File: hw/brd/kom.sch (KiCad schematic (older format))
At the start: 102 parts, among them IC1 ATMEGA328-P, IC2 4067D, IC3 L293D, J1 EXT, K1 CONN_3, M1 XBEE, P1 Serial, P10 GPIO_4PIN, P11 GPIO_4PIN, P12 GPIO_4PIN, P13 GPIO_4PIN, P14 GPIO_4PIN, P15 GPIO_4PIN, P16 GPIO_4PIN, P2 GPIO_4PIN, P3 GPIO_4PIN, P4 GPIO_4PIN, P5 GPIO_4PIN, P6 GPIO_4PIN, P7 GPIO_4PIN, P8 IR_Scanner, P9 GPIO_4PIN, Q1 PT480F, Q2 PT480F, Q3 PT480F, Q4 PT480F, SW1 SW_RESET, SW2 PwrOn, SW3 PWR_Control, SW4 TEST, U1 INDUCTOR, U2 LM7833, U3 74LS125, U4 TC54, U5 PTH08000WAZT, U6 ULN2003A, X1 16MHz

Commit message: - Changed schematic notation - Standard footprints linked
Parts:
- removed BypCCap2: MotorR, symbol C
- removed SW1: SW_RESET, symbol SW_PUSH
- removed SW4: TEST, symbol SW_PUSH
- added C?: 100nF MotorR, symbol C
- added SW1: SW_RESET, symbol PULSADOR
- added SW4: TEST, symbol PULSADOR
- C?: renamed from BypCCap1; value MotorL -> 100nF MotorL
- CAP?: renamed from H_Cap1; value 100uF -> 100uF HBridge
- CAP?: renamed from IR_Cap1; value 10uF -> 10uF IR
- CAP?: renamed from US_Cap1; value 10uF -> 10uF US
- CAP?: renamed from Mux_Cap1; value 100nF -> 100nF Mux
- CAP?: renamed from InCap1; value 100uF -> 100uF InCap
- CAP?: renamed from RadioCCap1; value 8.2pF -> 8.2pF Radio
- CAP?: renamed from RadioECap1; value 1uF -> 1uF Radio
- CAP?: renamed from AVCC_Cap1; value 100n -> 100n AVCC
- CAP?: renamed from AVR_Cap1; value 100n -> 100n AVR
- InvPolDiode1: value 200mA min -> 200mA IPP
- J?: renamed from K1; value CONN_3 -> LiPo
- P?: renamed from AREF1; value CONN_1 -> ARef
- renumbered I2 to I2C?, I1 to I2C?
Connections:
- wire segments 350 -> 267

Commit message: - Created new modules: 	Bluetooth 	LED_IR_Side 	JST_XH 	IR_PHT_Side 	PTH08000 	Ultrasonic sensor - Associated components
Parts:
- gave numbers to parts that had none: 15
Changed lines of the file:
@@
-EESchema Schematic File Version 2  date Mon 25 Jun 2012 08:07:17 PM CEST
+EESchema Schematic File Version 2  date Mon 25 Jun 2012 08:58:39 PM CEST
 LIBS:power
 LIBS:device
@@
 $EndComp
 $Comp
-L CONN_1 P?
+L CONN_1 P17
 U 1 1 4FD082B3
 P 3000 5000
-F 0 "P?" H 3080 5000 40  0000 L CNN
+F 0 "P17" H 3080 5000 40  0000 L CNN
 F 1 "ARef" H 3000 5055 29  0000 C CNN
 	1    3000 5000
@@
 $EndComp
 $Comp
-L JP_4 I2C?
+L JP_4 I2C2
 U 1 1 4FE2F5BD
 P 2750 9800
-F 0 "I2C?" H 2910 10020 58  0000 C CNN
+F 0 "I2C2" H 2910 10020 58  0000 C CNN
 F 1 "JP_4" H 2900 9740 60  0001 C CNN
 	1    2750 9800
@@
 $EndComp
 $Comp
-L JP_4 I2C?
+L JP_4 I2C1
 U 1 1 4FE2F5D4
 P 2250 9800
-F 0 "I2C?" H 2410 10020 58  0000 C CNN
+F 0 "I2C1" H 2410 10020 58  0000 C CNN
 F 1 "JP_4" H 2400 9740 60  0001 C CNN
 	1    2250 9800
@@
 $EndComp
 $Comp
-L CPOL CAP?
+L CPOL CAP3
 U 1 1 4FE2FF90
 P 8850 6750
-F 0 "CAP?" H 8950 6900 50  0000 L CNN
+F 0 "CAP3" H 8950 6900 50  0000 L CNN
 F 1 "100uF HBridge" H 8750 6600 50  0000 L CNN
 	1    8850 6750
@@
 $EndComp
 $Comp
-L CPOL CAP?
+L CPOL CAP2
 U 1 1 4FE2FF96
 P 8450 6750
-F 0 "CAP?" H 8550 6900 50  0000 L CNN
+F 0 "CAP2" H 8550 6900 50  0000 L CNN
 F 1 "10uF IR" H 8500 6600 50  0000 L CNN
 	1    8450 6750
@@
 $EndComp
 $Comp
-L CPOL CAP?
+L CPOL CAP4
 U 1 1 4FE2FFB0
 P 9250 6750
-F 0 "CAP?" H 9350 6900 50  0000 L CNN
+F 0 "CAP4" H 9350 6900 50  0000 L CNN
 F 1 "10uF US" H 9300 6600 50  0000 L CNN
 	1    9250 6750
@@
 $EndComp
 $Comp
-L CPOL CAP?
+L CPOL CAP5
 U 1 1 4FE2FFB6
 P 9650 6750
-F 0 "CAP?" H 9750 6900 50  0000 L CNN
+F 0 "CAP5" H 9750 6900 50  0000 L CNN
 F 1 "100nF Mux" H 9650 6600 50  0000 L CNN
 	1    9650 6750
@@
 	8450 6300 8450 6400
 $Comp
-L C C?
+L C C5
 U 1 1 4FE84566
 P 13250 9400
-F 0 "C?" V 13100 9350 50  0000 L CNN
+F 0 "C5" V 13100 9350 50  0000 L CNN
 F 1 "100nF MotorL" V 13400 9150 50  0000 L CNN
 	1    13250 9400
@@
 Connection ~ 15250 9700
 $Comp
-L CONN_3 J?
+L CONN_3 J2
 U 1 1 4FE85361
 P 1200 2200
-F 0 "J?" V 1150 2200 50  0000 C CNN
+F 0 "J2" V 1150 2200 50  0000 C CNN
 F 1 "LiPo" V 1250 2200 40  0000 C CNN
 	1    1200 2200
@@
 $EndComp
 $Comp
-L CPOL CAP?
+L CPOL CAP1
 U 1 1 4FE85957
 P 4650 2050
-F 0 "CAP?" H 4700 2200 50  0000 L CNN
+F 0 "CAP1" H 4700 2200 50  0000 L CNN
 F 1 "100uF InCap" H 4650 1900 50  0000 L CNN
 	1    4650 2050
@@
 	9650 6300 9650 6400
 $Comp
-L C CAP?
+L C CAP9
 U 1 1 4FE85D74
 P 11300 6550
-F 0 "CAP?" V 11150 6400 50  0000 L CNN
+F 0 "CAP9" V 11150 6400 50  0000 L CNN
 F 1 "8.2pF Radio" V 11450 6300 50  0000 L CNN
 	1    11300 6550
@@
 $EndComp
 $Comp
-L CPOL CAP?
+L CPOL CAP8
 U 1 1 4FE85D81
 P 10900 6750
-F 0 "CAP?" H 11000 6900 50  0000 L CNN
+F 0 "CAP8" H 11000 6900 50  0000 L CNN
 F 1 "1uF Radio" H 10900 6600 50  0000 L CNN
 	1    10900 6750
@@
 $EndComp
 $Comp
-L C CAP?
+L C CAP7
 U 1 1 4FE85DC0
 P 10500 6550
-F 0 "CAP?" V 10350 6450 50  0000 L CNN
+F 0 "CAP7" V 10350 6450 50  0000 L CNN
 F 1 "100n AVCC" V 10650 6350 50  0000 L CNN
 	1    10500 6550
@@
 Connection ~ 10900 6850
 $Comp
-L C CAP?
+L C CAP6
 U 1 1 4FE874B6
 P 10100 6550
-F 0 "CAP?" V 9950 6450 50  0000 L CNN
+F 0 "CAP6" V 9950 6450 50  0000 L CNN
 F 1 "100n AVR" V 10250 6350 50  0000 L CNN
 	1    10100 6550
@@
 $EndComp
 $Comp
-L C C?
+L C C6
 U 1 1 4FE8BAFD
 P 15250 9400
-F 0 "C?" V 15100 9350 50  0000 L CNN
+F 0 "C6" V 15100 9350 50  0000 L CNN
 F 1 "100nF MotorR" V 15400 9150 50  0000 L CNN
 	1    15250 9400

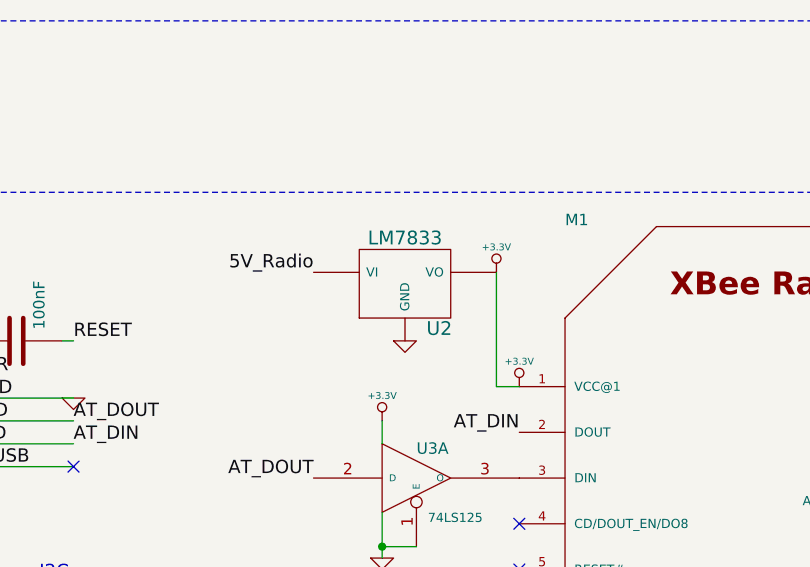
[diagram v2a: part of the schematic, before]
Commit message: - Changed 3.3V regulator symbol for a new one in kom lib - Fixed some association problems
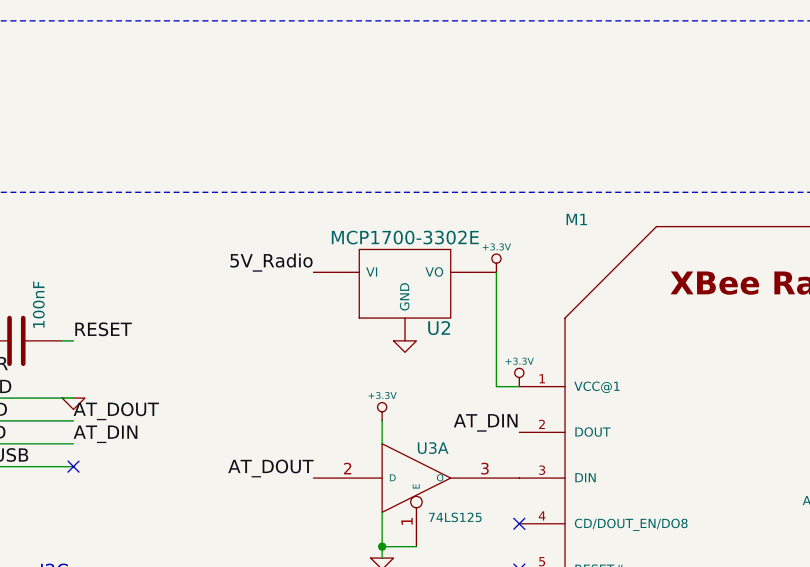
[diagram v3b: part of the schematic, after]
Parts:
- removed U2: LM7833, symbol LM7805
- added U2: MCP1700-3302E, symbol MCP1700-3302E
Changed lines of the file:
@@
-EESchema Schematic File Version 2  date Mon 25 Jun 2012 08:58:39 PM CEST
+EESchema Schematic File Version 2  date Tue 26 Jun 2012 11:47:49 AM CEST
 LIBS:power
 LIBS:device
@@
 Sheet 1 1
 Title "komBOT"
-Date "25 jun 2012"
+Date "26 jun 2012"
 Rev ""
 Comp "Universidad Carlos III"
@@
 F 2 "xbee_r1-XBEE" H 5050 9400 50  0001 C CNN
 	1    5050 9250
-	1    0    0    -1
-$EndComp
-$Comp
-L LM7805 U2
-U 1 1 4FD32BAA
-P 3550 8200
-F 0 "U2" H 3700 8004 60  0000 C CNN
-F 1 "LM7833" H 3550 8400 60  0000 C CNN
-	1    3550 8200
 	1    0    0    -1
 $EndComp
@@
 	1    0    0    -1
 $EndComp
+$Comp
+L MCP1700-3302E U2
+U 1 1 4FE984EB
+P 3550 8200
+F 0 "U2" H 3700 8004 59  0000 C CNN
+F 1 "MCP1700-3302E" H 3550 8400 58  0000 C CNN
+	1    3550 8200
+	1    0    0    -1
+$EndComp

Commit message: - Changed some schematic notation - Started placing modules
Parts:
- I2C1, I2C2: value JP_4 -> I2C
- P10: value GPIO_4PIN -> X1
- P11: value GPIO_4PIN -> X2
- P12: value GPIO_4PIN -> X3
- P13: value GPIO_4PIN -> X4
- P14: value GPIO_4PIN -> X5
- P15: value GPIO_4PIN -> X6
- P16: value GPIO_4PIN -> X7
- P2: value GPIO_4PIN -> D2
- P3: value GPIO_4PIN -> D5
- P4: value GPIO_4PIN -> D6
- P5: value GPIO_4PIN -> A1
- P6: value GPIO_4PIN -> A2
- P7: value GPIO_4PIN -> A3
- P9: value GPIO_4PIN -> X0
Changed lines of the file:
@@
-EESchema Schematic File Version 2  date Tue 26 Jun 2012 11:47:49 AM CEST
+EESchema Schematic File Version 2  date Tue 26 Jun 2012 01:58:56 PM CEST
 LIBS:power
 LIBS:device
@@
 P 8650 4400
 F 0 "P2" H 9100 4400 60  0000 C CNN
-F 1 "GPIO_4PIN" H 8650 4550 59  0001 C CNN
+F 1 "D2" H 8650 4550 58  0001 C CNN
 	1    8650 4400
 	1    0    0    -1
@@
 P 8650 4600
 F 0 "P3" H 9100 4600 60  0000 C CNN
-F 1 "GPIO_4PIN" H 8650 4750 59  0001 C CNN
+F 1 "D5" H 8650 4750 58  0001 C CNN
 	1    8650 4600
 	1    0    0    -1
@@
 P 8650 4800
 F 0 "P4" H 9100 4800 60  0000 C CNN
-F 1 "GPIO_4PIN" H 8650 4950 59  0001 C CNN
+F 1 "D6" H 8650 4950 58  0001 C CNN
 	1    8650 4800
 	1    0    0    -1
@@
 P 8650 5000
 F 0 "P5" H 9100 5000 60  0000 C CNN
-F 1 "GPIO_4PIN" H 8650 5150 59  0001 C CNN
+F 1 "A1" H 8650 5150 58  0001 C CNN
 	1    8650 5000
 	1    0    0    -1
@@
 P 8650 5200
 F 0 "P6" H 9100 5200 60  0000 C CNN
-F 1 "GPIO_4PIN" H 8650 5350 59  0001 C CNN
+F 1 "A2" H 8650 5350 58  0001 C CNN
 	1    8650 5200
 	1    0    0    -1
@@
 P 8650 5400
 F 0 "P7" H 9100 5400 60  0000 C CNN
-F 1 "GPIO_4PIN" H 8650 5550 59  0001 C CNN
+F 1 "A3" H 8650 5550 58  0001 C CNN
 	1    8650 5400
 	1    0    0    -1
@@
 P 14850 1500
 F 0 "P9" H 15300 1500 60  0000 C CNN
-F 1 "GPIO_4PIN" H 14850 1650 59  0001 C CNN
+F 1 "X0" H 14850 1650 58  0001 C CNN
 	1    14850 1500
 	1    0    0    -1
@@
 P 14850 1700
 F 0 "P10" H 15300 1700 60  0000 C CNN
-F 1 "GPIO_4PIN" H 14850 1850 59  0001 C CNN
+F 1 "X1" H 14850 1850 58  0001 C CNN
 	1    14850 1700
 	1    0    0    -1
@@
 P 14850 1900
 F 0 "P11" H 15300 1900 60  0000 C CNN
-F 1 "GPIO_4PIN" H 14850 2050 59  0001 C CNN
+F 1 "X2" H 14850 2050 58  0001 C CNN
 	1    14850 1900
 	1    0    0    -1
@@
 P 14850 2100
 F 0 "P12" H 15300 2100 60  0000 C CNN
-F 1 "GPIO_4PIN" H 14850 2250 59  0001 C CNN
+F 1 "X3" H 14850 2250 58  0001 C CNN
 	1    14850 2100
 	1    0    0    -1
@@
 P 14850 2300
 F 0 "P13" H 15300 2300 60  0000 C CNN
-F 1 "GPIO_4PIN" H 14850 2450 59  0001 C CNN
+F 1 "X4" H 14850 2450 58  0001 C CNN
 	1    14850 2300
 	1    0    0    -1
@@
 P 14850 2500
 F 0 "P14" H 15300 2500 60  0000 C CNN
-F 1 "GPIO_4PIN" H 14850 2650 59  0001 C CNN
+F 1 "X5" H 14850 2650 58  0001 C CNN
 	1    14850 2500
 	1    0    0    -1
@@
 P 14850 2700
 F 0 "P15" H 15300 2700 60  0000 C CNN
-F 1 "GPIO_4PIN" H 14850 2850 59  0001 C CNN
+F 1 "X6" H 14850 2850 58  0001 C CNN
 	1    14850 2700
 	1    0    0    -1
@@
 P 14850 2900
 F 0 "P16" H 15300 2900 60  0000 C CNN
-F 1 "GPIO_4PIN" H 14850 3050 59  0001 C CNN
+F 1 "X7" H 14850 3050 58  0001 C CNN
 	1    14850 2900
 	1    0    0    -1
@@
 P 2750 9800
 F 0 "I2C2" H 2910 10020 58  0000 C CNN
-F 1 "JP_4" H 2900 9740 60  0001 C CNN
+F 1 "I2C" H 2900 9740 59  0001 C CNN
 	1    2750 9800
 	0    1    1    0
@@
 P 2250 9800
 F 0 "I2C1" H 2410 10020 58  0000 C CNN
-F 1 "JP_4" H 2400 9740 60  0001 C CNN
+F 1 "I2C" H 2400 9740 59  0001 C CNN
 	1    2250 9800
 	0    1    1    0

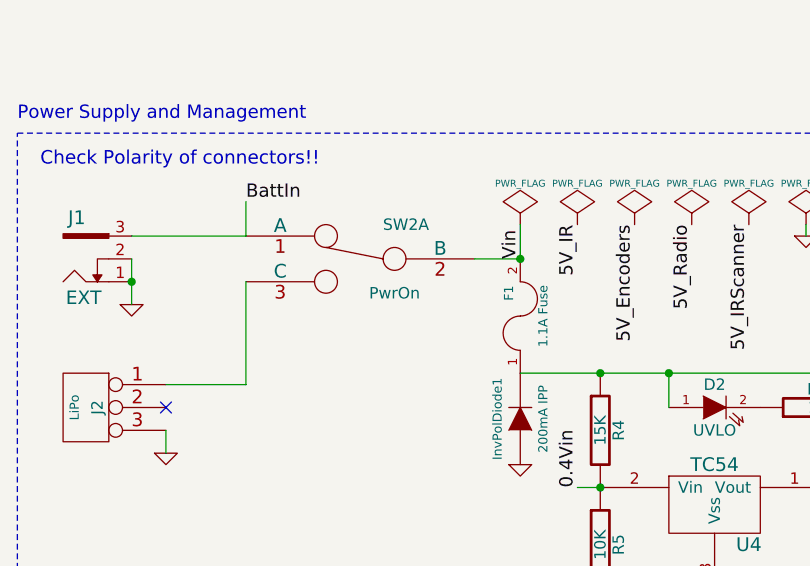
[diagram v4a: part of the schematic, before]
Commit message: - Placed POWER components
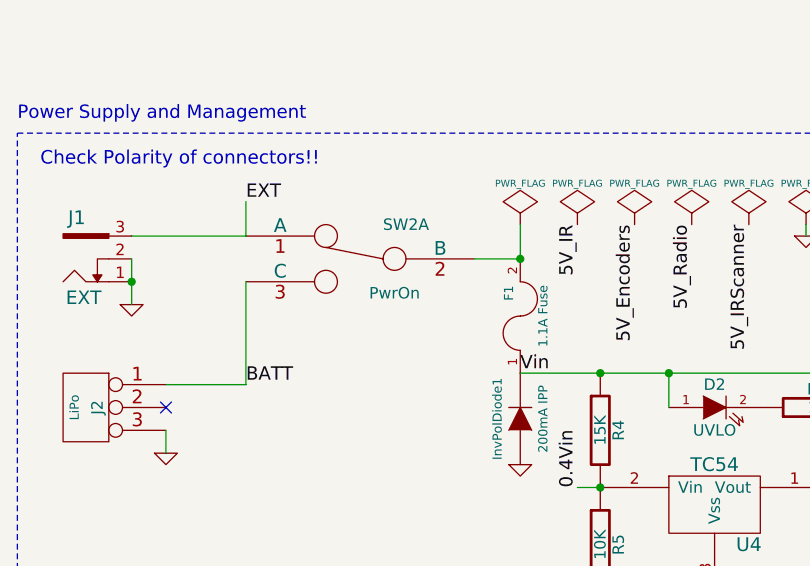
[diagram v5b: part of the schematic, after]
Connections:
- net labels added: BATT, EXT
- net labels removed: BattIn
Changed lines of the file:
@@
-EESchema Schematic File Version 2  date Tue 26 Jun 2012 01:58:56 PM CEST
+EESchema Schematic File Version 2  date Tue 26 Jun 2012 05:34:39 PM CEST
 LIBS:power
 LIBS:device
@@
 $EndComp
 Text Label 1900 1300 0    58   ~ 0
-BattIn
+EXT
 Text Notes 900  950  0    58   ~ 0
 Power Supply and Management
@@
 Text Label 3350 2550 1    58   ~ 0
 0.4Vin
-Text Label 3100 1550 1    58   ~ 0
+Text Label 3100 2050 0    58   ~ 0
 Vin
 $Comp
@@
 	1    0    0    -1
 $EndComp
+Text Label 1900 2100 0    58   ~ 0
+BATT
 $EndSCHEMATC
